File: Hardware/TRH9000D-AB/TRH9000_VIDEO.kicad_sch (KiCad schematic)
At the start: 47 parts, among them J1 Norcomp_200-015-263R001, J2 Console5_SCART, U10 THS7374-lrj, U6 LMH1980, U7 AD8188

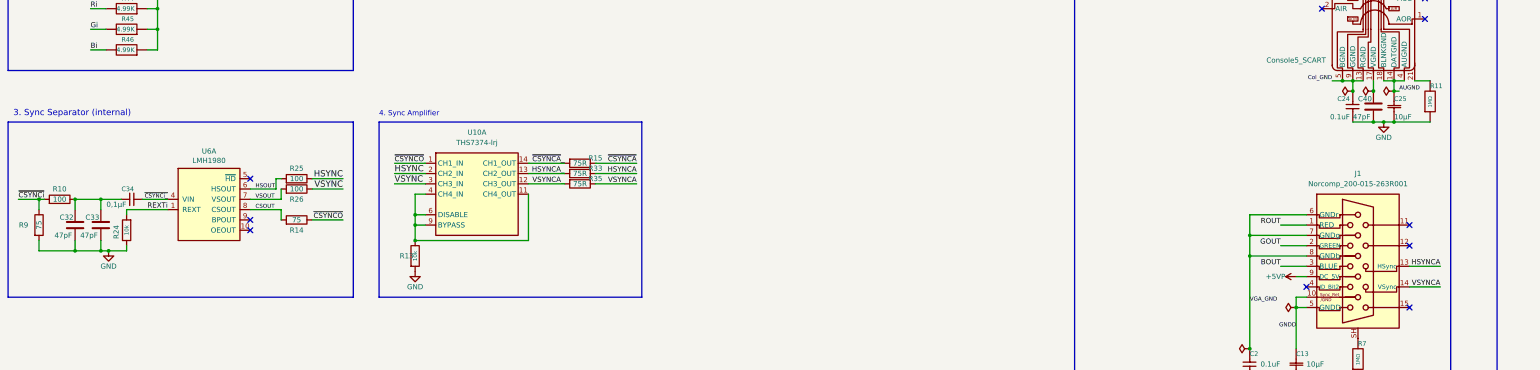
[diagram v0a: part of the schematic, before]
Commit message: Finished rerouting the AA-variant, and replaced the fuses with SMD-ones.
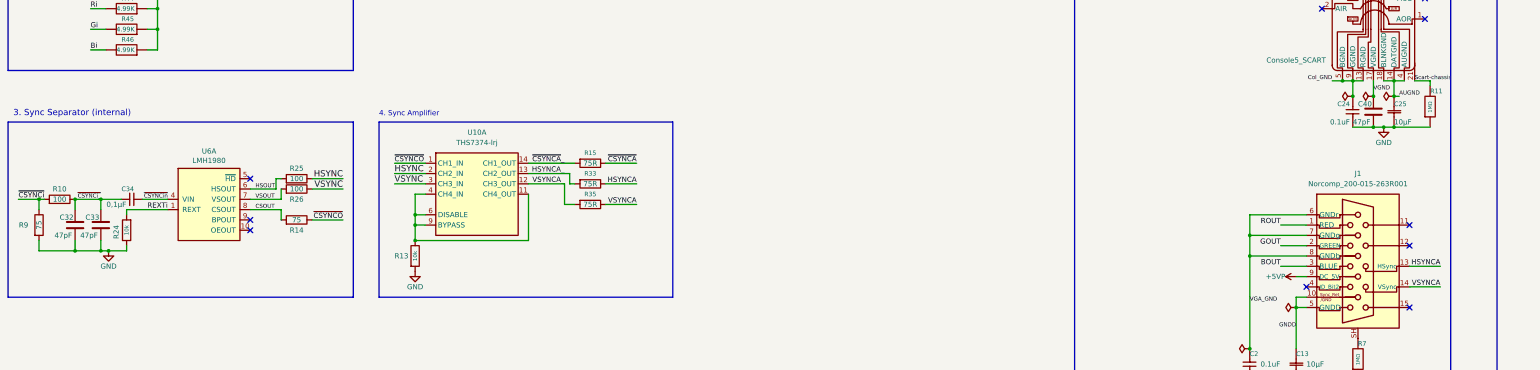
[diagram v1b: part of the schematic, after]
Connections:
- net ~{CSYNCi_}: now also C32.1, C33.1, C34.2, R10.1; no longer C34.1, U6.4 (VIN)
- net VGND: now reaches C40.1, J2.17 (VGND)
- net Scart-chassis: now reaches J2.21 (SH), R11.2
- new net ~{CSYNCin}: C34.1, U6.4 (VIN)
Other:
- moved on the sheet: C24, C25, C40, R11, R15, R33, R35
